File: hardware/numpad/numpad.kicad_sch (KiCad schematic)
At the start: 0 parts

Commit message: fp-lib-table change plus schematic
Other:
- added sheet 01_power_usb (01_power_usb.kicad_sch)
- added sheet 02_mcu (02_mcu.kicad_sch)
- added sheet 03_matrix (03_matrix.kicad_sch)
- added sheet 04_rgb (04_rgb.kicad_sch)
- added sheet 05_ui (05_ui.kicad_sch)
- title: (none) -> Numpad PCB Schematic
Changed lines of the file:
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@@
 	(generator_version "10.0")
 	(paper "A4")
+	(title_block
+		(title "Numpad PCB Schematic")
+		(date "2026-07-15")
+		(rev "0")
+	)
+	(sheet
+		(at 27.94 156.21)
+		(size 12.7 11.43)
+		(exclude_from_sim no)
+		(in_bom yes)
+		(on_board yes)
+		(dnp no)
+		(fields_autoplaced yes)
+		(stroke
+			(width 0.1524)
+			(type solid)
+		)
+		(fill
+			(color 0 0 0 0)
+		)
+		(property "Sheetname" "01_power_usb"
+			(at 27.94 155.4984 0)
+			(show_name no)
+			(do_not_autoplace no)
+			(effects
+				(font
+					(size 1.27 1.27)
+				)
+				(justify left bottom)
+			)
+		)
+		(property "Sheetfile" "01_power_usb.kicad_sch"
+			(at 27.94 168.2246 0)
+			(show_name no)
+			(do_not_autoplace no)
+			(effects
+				(font
+					(size 1.27 1.27)
+				)
+				(justify left top)
+			)
+		)
+		(instances
+			(project "numpad"
+				(path "/a21b85ed-e0a7-4fe0-8fc3-9355226ce8a2"
+					(page "2")
+				)
+			)
+		)
+	)
+	(sheet
+		(at 83.82 156.21)
+		(size 12.7 11.43)
+		(exclude_from_sim no)
+		(in_bom yes)
+		(on_board yes)
+		(dnp no)
+		(fields_autoplaced yes)
+		(stroke
+			(width 0.1524)
+			(type solid)
+		)
+		(fill
+			(color 0 0 0 0)
+		)
+		(property "Sheetname" "03_matrix"
+			(at 83.82 155.4984 0)
+			(show_name no)
+			(do_not_autoplace no)
+			(effects
+				(font
+					(size 1.27 1.27)
+				)
+				(justify left bottom)
+			)
+		)
+		(property "Sheetfile" "03_matrix.kicad_sch"
+			(at 83.82 168.2246 0)
+			(show_name no)
+			(do_not_autoplace no)
+			(effects
+				(font
+					(size 1.27 1.27)
+				)
+				(justify left top)
+			)
+		)
+		(instances
+			(project "numpad"
+				(path "/a21b85ed-e0a7-4fe0-8fc3-9355226ce8a2"
+					(page "4")
+				)
+			)
+		)
+	)
+	(sheet
+		(at 58.42 156.21)
+		(size 12.7 11.43)
+		(exclude_from_sim no)
+		(in_bom yes)
+		(on_board yes)
+		(dnp no)
+		(fields_autoplaced yes)
+		(stroke
+			(width 0.1524)
+			(type solid)
+		)
+		(fill
+			(color 0 0 0 0)
+		)
+		(property "Sheetname" "02_mcu"
+			(at 58.42 155.4984 0)
+			(show_name no)
+			(do_not_autoplace no)
+			(effects
+				(font
+					(size 1.27 1.27)
+				)
+				(justify left bottom)
+			)
+		)
+		(property "Sheetfile" "02_mcu.kicad_sch"
+			(at 58.42 168.2246 0)
+			(show_name no)
+			(do_not_autoplace no)
+			(effects
+				(font
+					(size 1.27 1.27)
+				)
+				(justify left top)
+			)
+		)
+		(instances
+			(project "numpad"
+				(path "/a21b85ed-e0a7-4fe0-8fc3-9355226ce8a2"
+					(page "3")
+				)
+			)
+		)
+	)
+	(sheet
+		(at 110.49 156.21)
+		(size 12.7 11.43)
+		(exclude_from_sim no)
+		(in_bom yes)
+		(on_board yes)
+		(dnp no)
+		(fields_autoplaced yes)
+		(stroke
+			(width 0.1524)
+			(type solid)
+		)
+		(fill
+			(color 0 0 0 0)
+		)
+		(property "Sheetname" "04_rgb"
+			(at 110.49 155.4984 0)
+			(show_name no)
+			(do_not_autoplace no)
+			(effects
+				(font
+					(size 1.27 1.27)
+				)
+				(justify left bottom)
+			)
+		)
+		(property "Sheetfile" "04_rgb.kicad_sch"
+			(at 110.49 168.2246 0)
+			(show_name no)
+			(do_not_autoplace no)
+			(effects
+				(font
+					(size 1.27 1.27)
+				)
+				(justify left top)
+			)
+		)
+		(instances
+			(project "numpad"
+				(path "/a21b85ed-e0a7-4fe0-8fc3-9355226ce8a2"
+					(page "5")
+				)
+			)
+		)
+	)
+	(sheet
+		(at 134.62 156.21)
+		(size 12.7 11.43)
+		(exclude_from_sim no)
+		(in_bom yes)
+		(on_board yes)
+		(dnp no)
+		(fields_autoplaced yes)
+		(stroke
+			(width 0.1524)
+			(type solid)
+		)
+		(fill
+			(color 0 0 0 0)
+		)
+		(property "Sheetname" "05_ui"
+			(at 134.62 155.4984 0)
+			(show_name no)
+			(do_not_autoplace no)
+			(effects
+				(font
+					(size 1.27 1.27)
+				)
+				(justify left bottom)
+			)
+		)
+		(property "Sheetfile" "05_ui.kicad_sch"
+			(at 134.62 168.2246 0)
+			(show_name no)
+			(do_not_autoplace no)
+			(effects
+				(font
+					(size 1.27 1.27)
+				)
+				(justify left top)
+			)
+		)
+		(instances
+			(project "numpad"
+				(path "/a21b85ed-e0a7-4fe0-8fc3-9355226ce8a2"
+					(page "6")
+				)
+			)
+		)
+	)
 	(sheet_instances
 		(path "/"

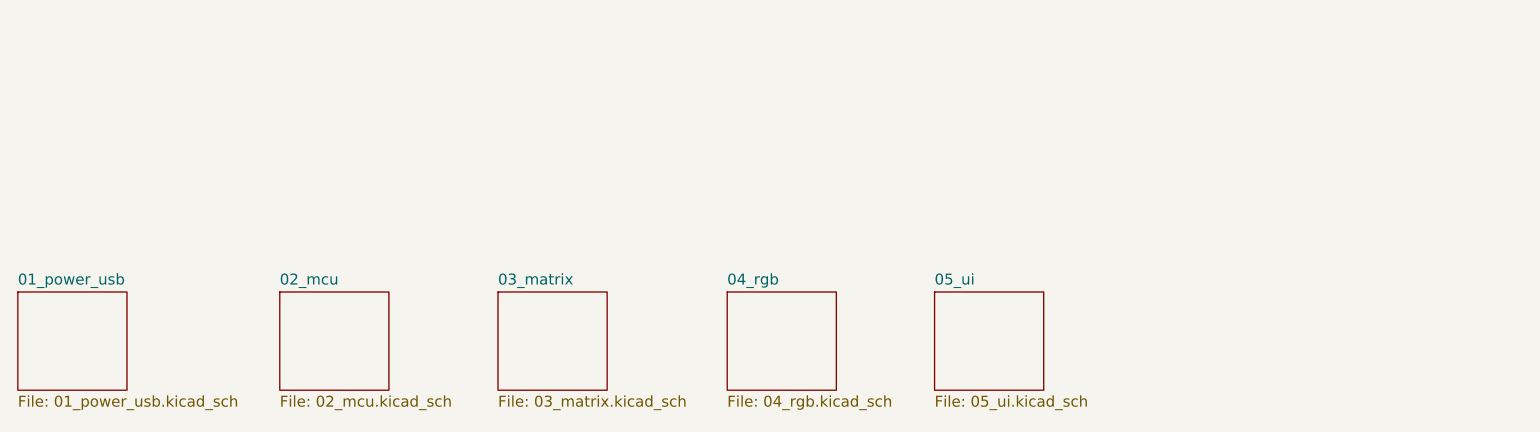
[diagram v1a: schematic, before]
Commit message: matrix sheet, encoder, root hierarchy wired
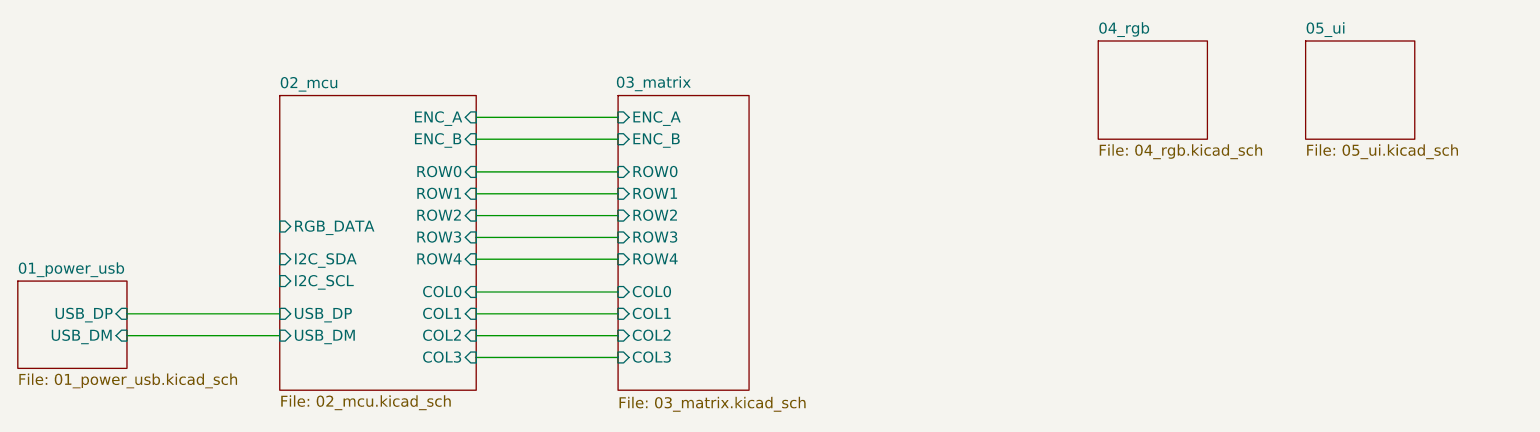
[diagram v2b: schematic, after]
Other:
- sheet 01_power_usb ports: added USB_DM, USB_DP; removed none
- sheet 02_mcu ports: added COL0, COL1, COL2, COL3, ENC_A, ENC_B, I2C_SCL, I2C_SDA, RGB_DATA, ROW0, ROW1, ROW2, ROW3, ROW4, USB_DM, USB_DP; removed none
- sheet 03_matrix ports: added COL0, COL1, COL2, COL3, ENC_A, ENC_B, ROW0, ROW1, ROW2, ROW3, ROW4; removed none

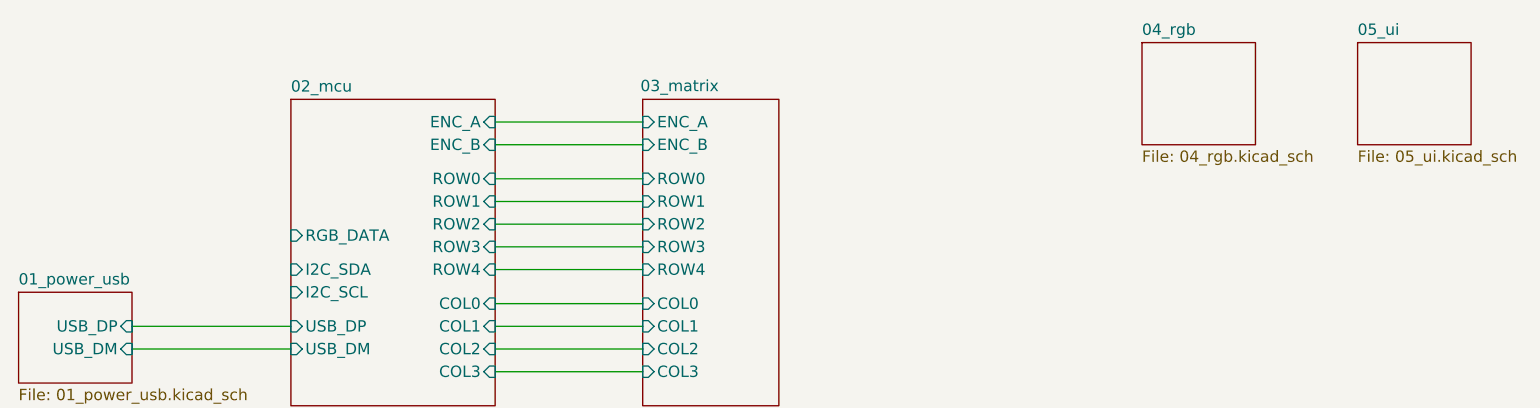
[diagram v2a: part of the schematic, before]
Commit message: RGB chain with level shifter
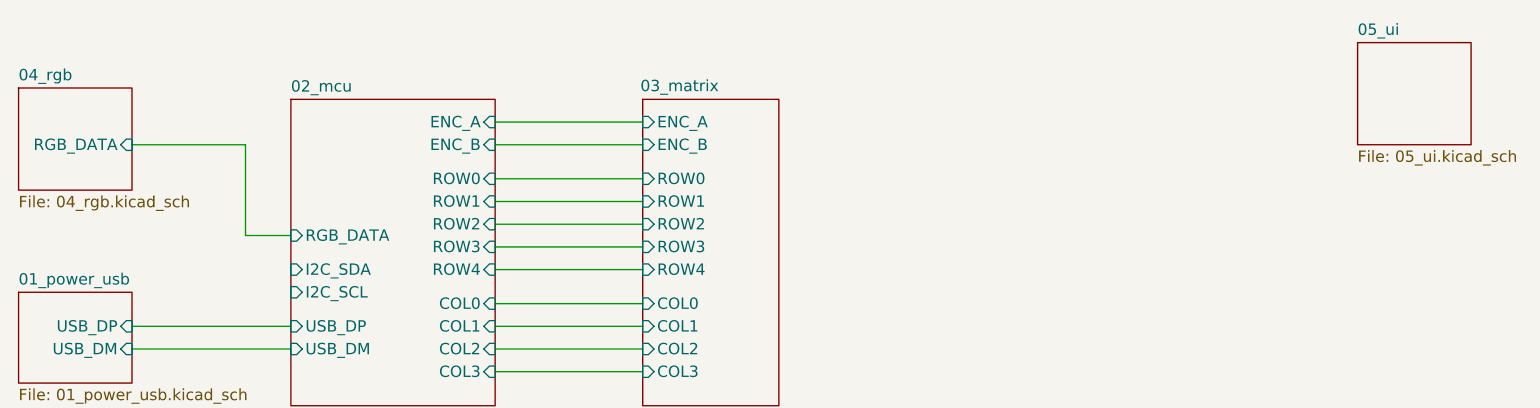
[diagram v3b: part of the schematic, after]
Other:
- sheet 04_rgb ports: added RGB_DATA; removed none
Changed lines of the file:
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@@
+	(wire
+		(pts
+			(xy 53.34 138.43) (xy 53.34 148.59)
+		)
+		(stroke
+			(width 0)
+			(type default)
+		)
+	)
 	(wire
 		(pts
@@
 	(wire
 		(pts
+			(xy 53.34 148.59) (xy 58.42 148.59)
+		)
+		(stroke
+			(width 0)
+			(type default)
+		)
+	)
+	(wire
+		(pts
 			(xy 81.28 152.4) (xy 97.79 152.4)
 		)
@@
 		(pts
 			(xy 81.28 144.78) (xy 97.79 144.78)
+		)
+		(stroke
+			(width 0)
+			(type default)
+		)
+	)
+	(wire
+		(pts
+			(xy 40.64 138.43) (xy 53.34 138.43)
 		)
 		(stroke
@@
 	)
 	(sheet
-		(at 153.67 127)
+		(at 27.94 132.08)
 		(size 12.7 11.43)
 		(exclude_from_sim no)
@@
 		)
 		(property "Sheetname" "04_rgb"
-			(at 153.67 126.2884 0)
+			(at 27.94 131.3684 0)
 			(show_name no)
 			(do_not_autoplace no)
@@
 		)
 		(property "Sheetfile" "04_rgb.kicad_sch"
-			(at 153.67 139.0146 0)
+			(at 27.94 144.0946 0)
 			(show_name no)
 			(do_not_autoplace no)
@@
 			)
 		)
+		(pin "RGB_DATA" input
+			(at 40.64 138.43 0)
+			(effects
+				(font
+					(size 1.27 1.27)
+				)
+				(justify right)
+			)
+		)

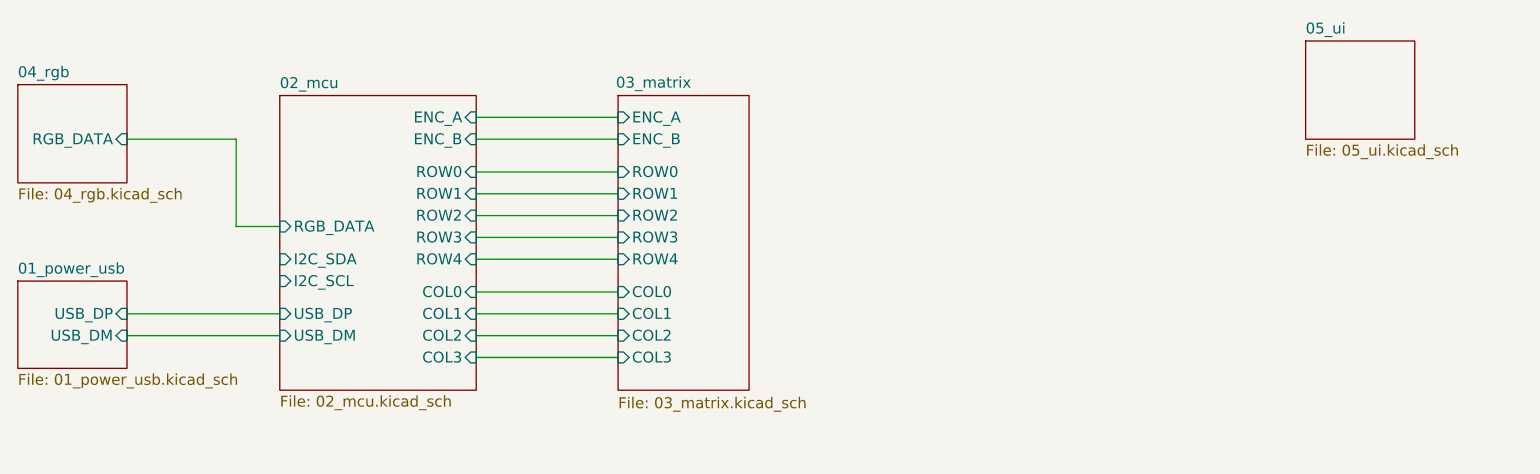
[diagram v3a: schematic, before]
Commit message: LCD header with I2C level shifting, schematic complete
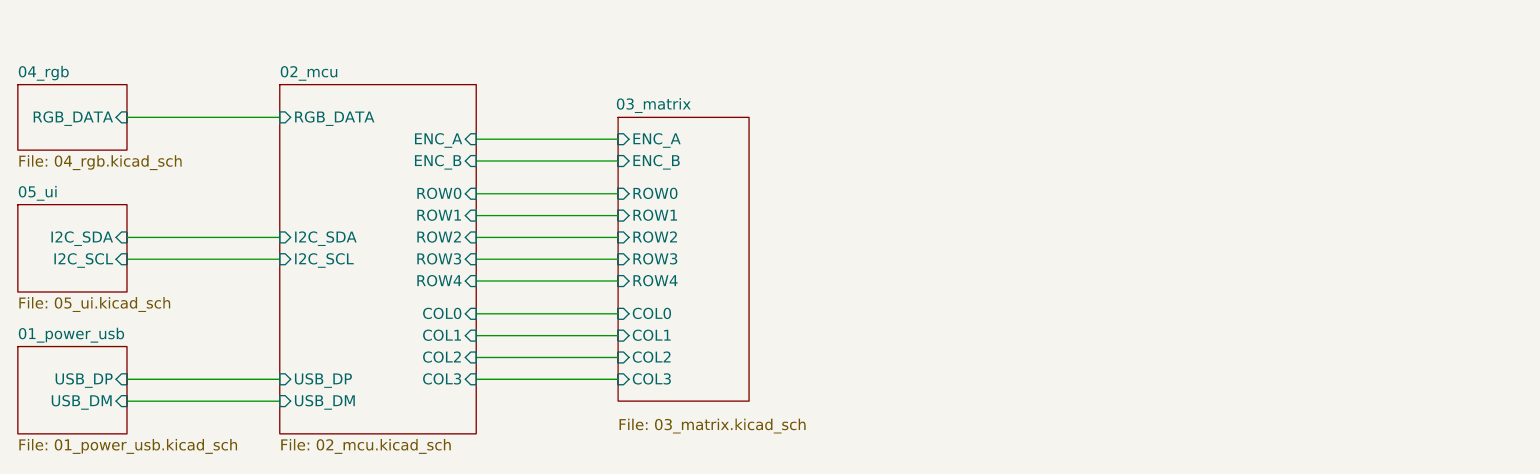
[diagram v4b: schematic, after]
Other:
- sheet 05_ui ports: added I2C_SCL, I2C_SDA; removed none
